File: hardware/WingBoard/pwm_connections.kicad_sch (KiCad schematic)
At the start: 11 parts

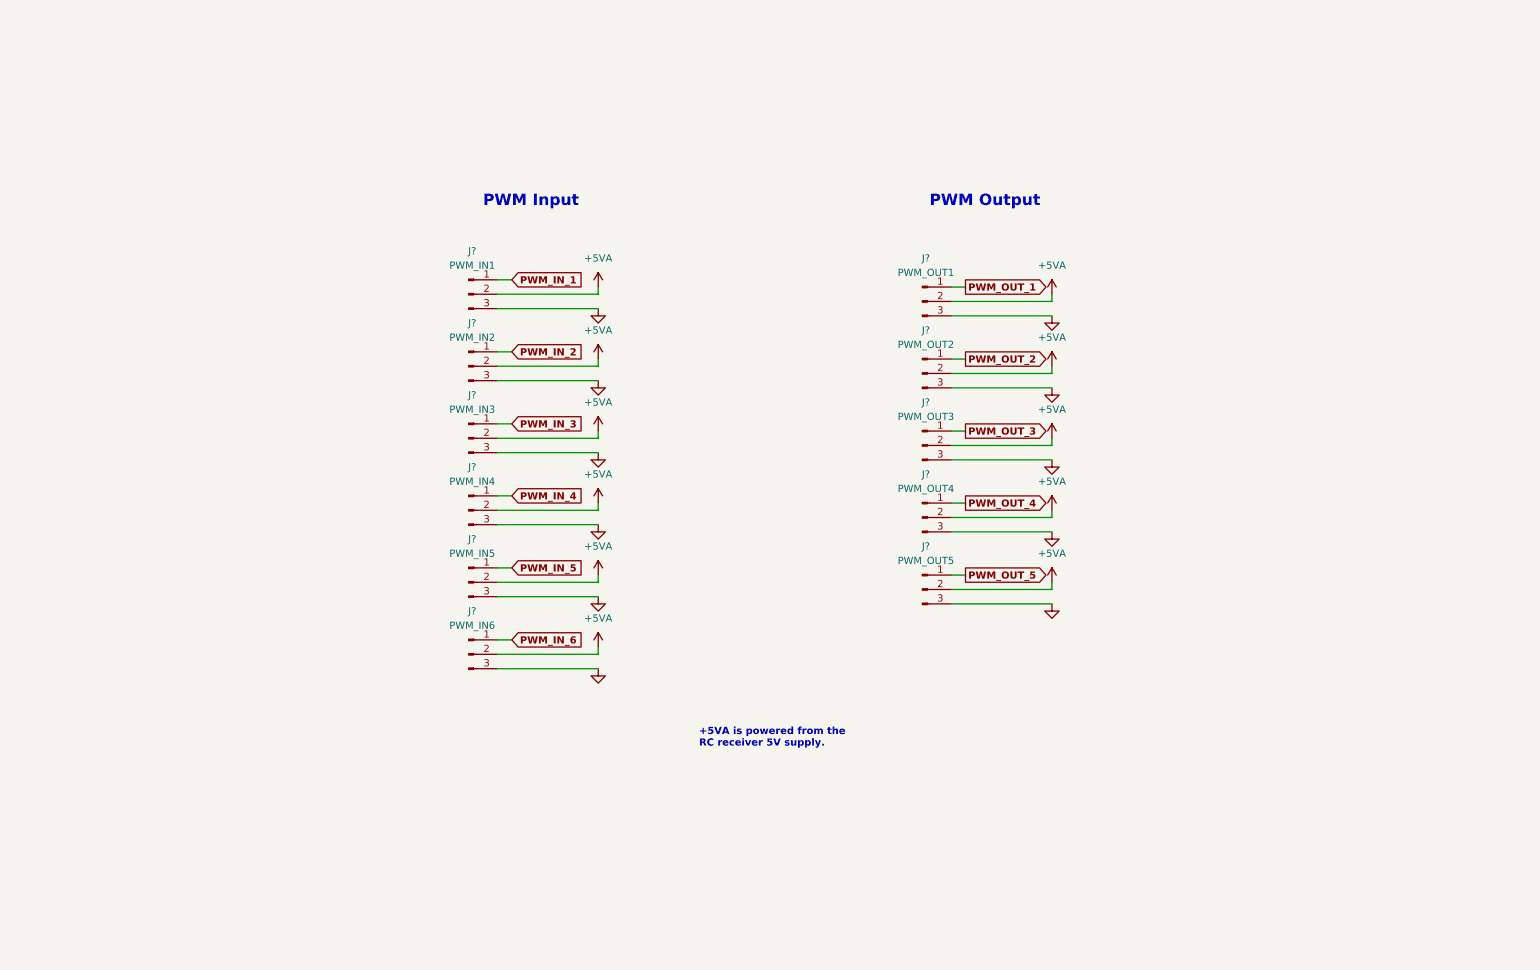
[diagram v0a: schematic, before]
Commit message: Added pwm controller.
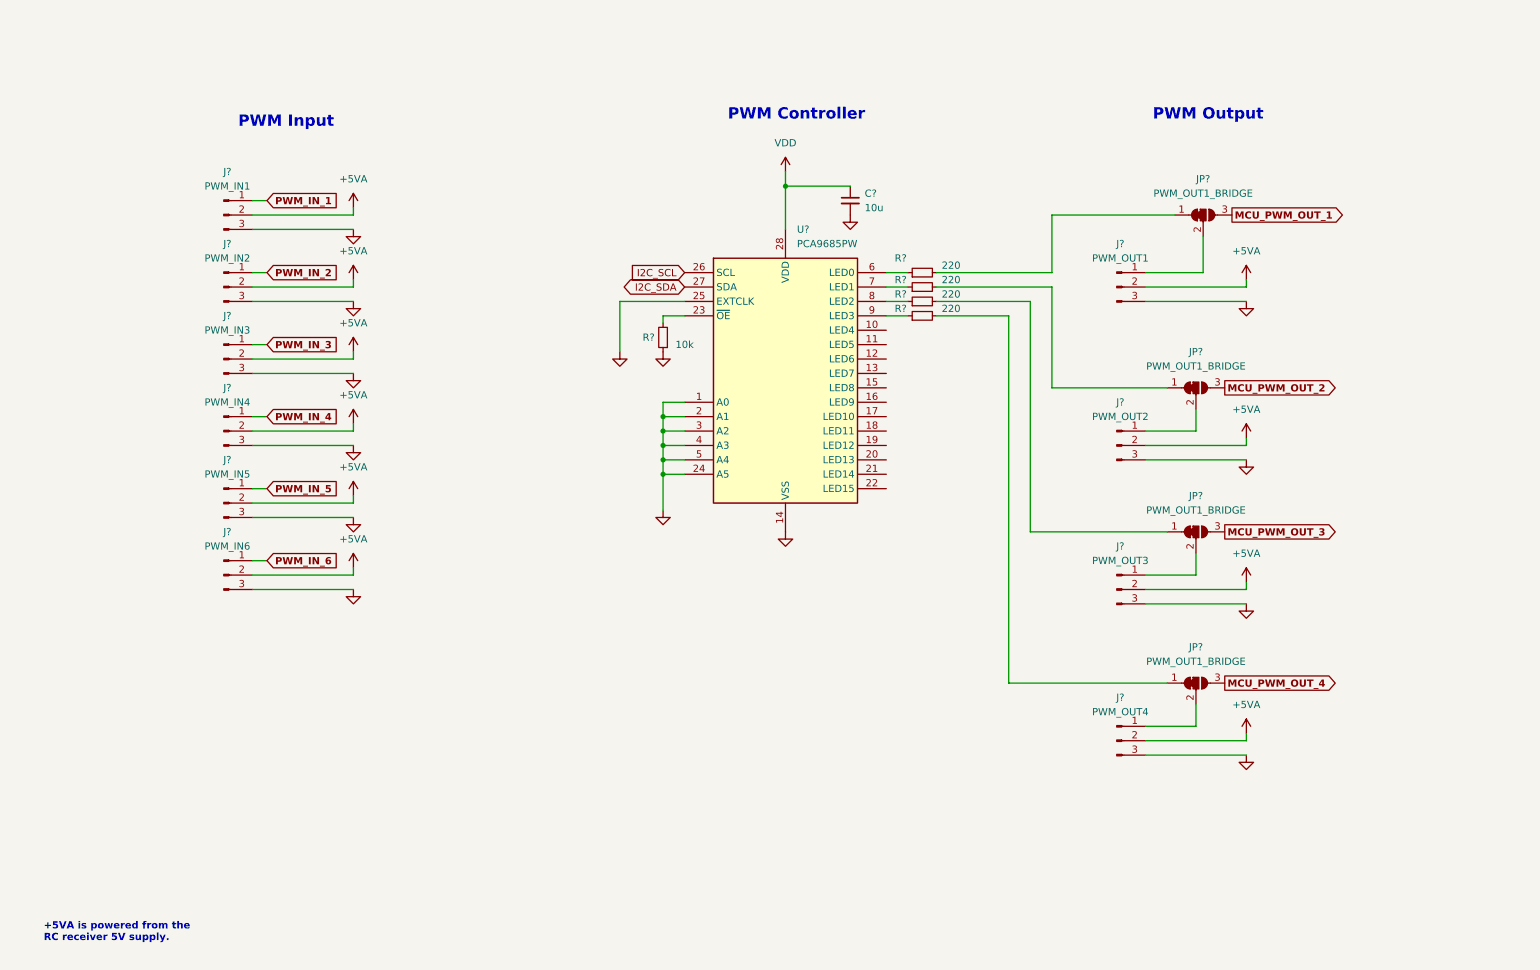
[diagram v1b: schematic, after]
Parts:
- removed J?: PWM_OUT5, symbol Connector:Conn_01x03_Male
- added C?: 10u, symbol Device:C_Small
- added JP? (x4): PWM_OUT1_BRIDGE, symbol Jumper:SolderJumper_3_Bridged12
- added R? (x4): 220, symbol Device:R_Small
- added R?: 10k, symbol Device:R_Small
- added U?: PCA9685PW, Package_SO:TSSOP-28_4.4x9.7mm_P0.65mm, symbol Driver_LED:PCA9685PW
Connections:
- net GND: now also C?.2, R?.1, U?.1 (A0), U?.14 (VSS), U?.2 (A1), U?.24 (A5), U?.25 (EXTCLK), U?.3 (A2), U?.4 (A3), U?.5 (A4)
- net PWM_OUT_1: no longer names the net of J?.1 (Pin_1)
- net PWM_OUT_1: now also JP?.2 (C)
- net PWM_OUT_2: no longer names the net of J?.1 (Pin_1)
- net PWM_OUT_2: now also JP?.2 (C)
- net PWM_OUT_3: no longer names the net of J?.1 (Pin_1)
- net PWM_OUT_3: now also JP?.2 (C)
- net PWM_OUT_4: no longer names the net of J?.1 (Pin_1)
- net PWM_OUT_4: now also JP?.2 (C)
- new net: JP?.1 (A), R?.2 (x4)
- new net: R?.2, U?.23 (~{OE})
- new net: R?.1, U?.6 (LED0)
- new net: R?.1, U?.7 (LED1)
- new net: R?.1, U?.8 (LED2)
- new net: R?.1, U?.9 (LED3)
- new net I2C_SCL: U?.26 (SCL)
- new net I2C_SDA: U?.27 (SDA)
- new net MCU_PWM_OUT_1: JP?.3 (B)
- new net MCU_PWM_OUT_2: JP?.3 (B)
- new net MCU_PWM_OUT_3: JP?.3 (B)
- new net MCU_PWM_OUT_4: JP?.3 (B)
- new net VDD: C?.1, U?.28 (VDD)
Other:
- note added: "PWM Controller"
- moved on the sheet: J?

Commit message: Hardware update: status LEDs, DIP switches, & test points.
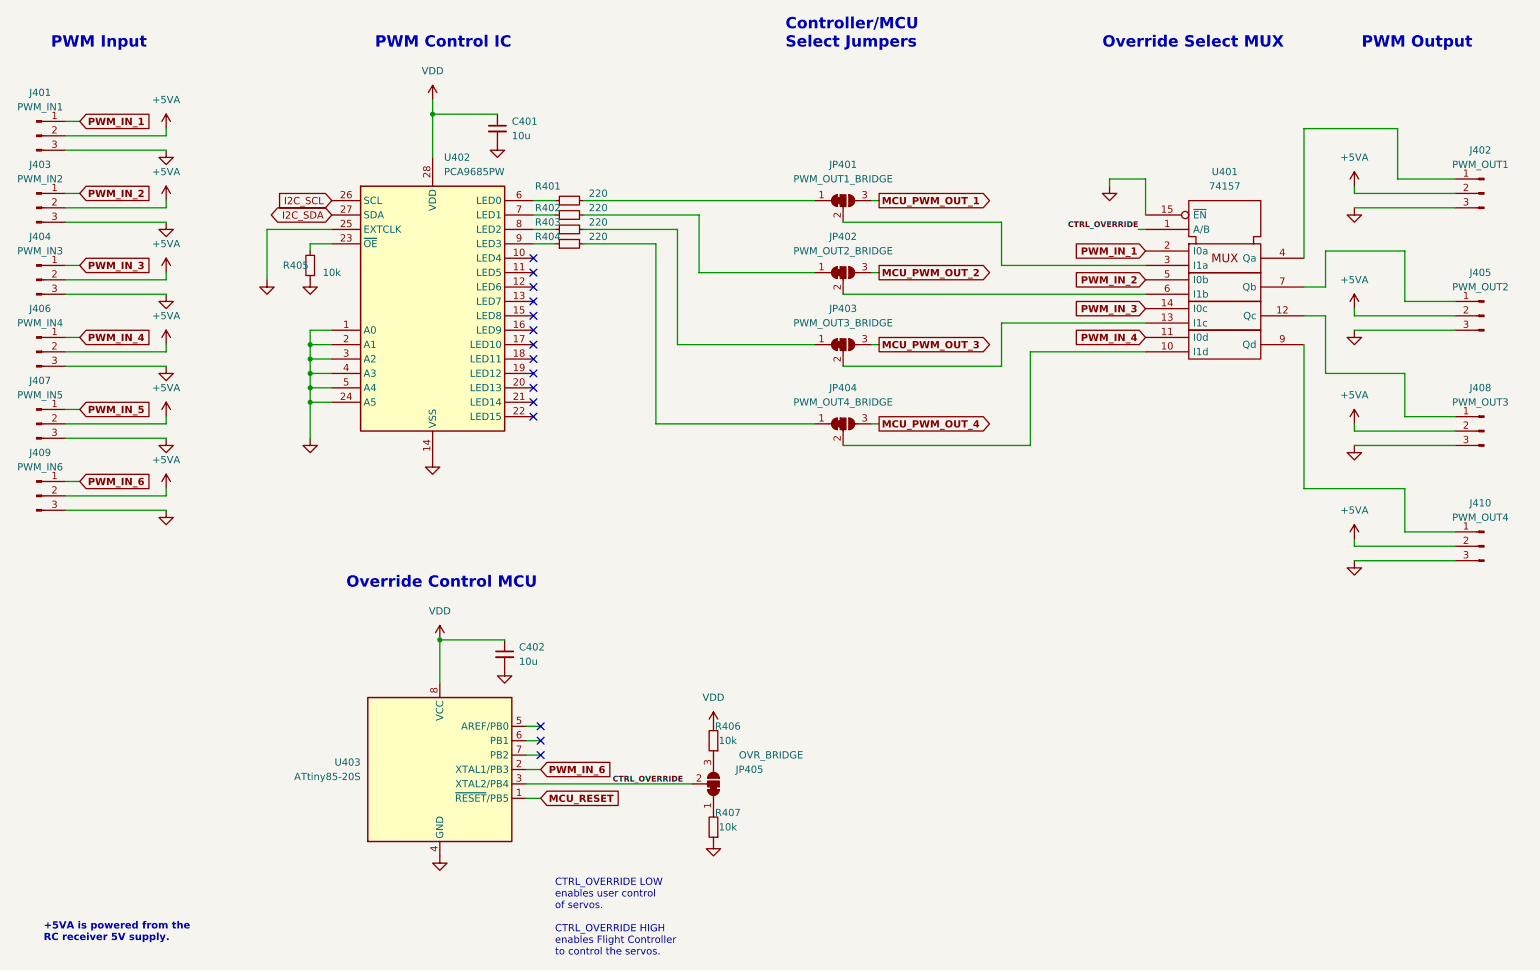
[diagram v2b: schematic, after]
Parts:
- added C402: 10u, symbol Device:C_Small
- added JP405: OVR_BRIDGE, symbol Jumper:SolderJumper_3_Bridged12
- added R406, R407: 10k, symbol Device:R_Small
- added U401: 74157, symbol 74xx_IEEE:74157
- added U403: ATtiny85-20S, Package_SO:SOIC-8W_5.3x5.3mm_P1.27mm, symbol MCU_Microchip_ATtiny:ATtiny85-20S
- JP402: renamed from JP?; value PWM_OUT1_BRIDGE -> PWM_OUT2_BRIDGE
- JP403: renamed from JP?; value PWM_OUT1_BRIDGE -> PWM_OUT3_BRIDGE
- JP404: renamed from JP?; value PWM_OUT1_BRIDGE -> PWM_OUT4_BRIDGE
- gave numbers to parts that had none: 18
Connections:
- net GND: now also C402.2, R407.1, U401.15 (~{EN}), U401.8 (GND), U403.4 (GND)
- net PWM_IN_1: now also U401.2 (I0a)
- net PWM_IN_2: now also U401.5 (I0b)
- net PWM_IN_3: now also U401.14 (I0c)
- net PWM_IN_4: now also U401.11 (I0d)
- net PWM_IN_6: now also U403.2 (XTAL1/PB3)
- net VDD: now also C402.1, R406.2, U403.8 (VCC)
- net at JP403.2 (C): now also U401.13 (I1c); no longer J408.1 (Pin_1)
- net at JP404.2 (C): now also U401.10 (I1d); no longer J410.1 (Pin_1)
- net at JP402.2 (C): now also U401.6 (I1b); no longer J405.1 (Pin_1)
- net at JP401.2 (C): now also U401.3 (I1a); no longer J402.1 (Pin_1)
- new net: JP405.1 (A), R407.2
- new net: JP405.3 (B), R406.1
- new net: J408.1 (Pin_1), U401.12 (Qc)
- new net: J402.1 (Pin_1), U401.4 (Qa)
- new net: J405.1 (Pin_1), U401.7 (Qb)
- new net: J410.1 (Pin_1), U401.9 (Qd)
- new net CTRL_OVERRIDE: JP405.2 (C), U401.1 (A/B), U403.3 (XTAL2/PB4)
- new net MCU_RESET: U403.1 (~{RESET}/PB5)
- new net VCC: U401.16 (VCC)
- no-connect marks 0 -> 15
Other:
- note added: "CTRL_OVERRIDE LOW enables user control of servos. CTRL_OVERRIDE HIGH enables Flight Controller to control the servos."
- note added: "Controller/MCU Select Jumpers"
- note added: "Override Control MCU"
- note added: "Override Select MUX"
- note added: "PWM Control IC"
- note removed: "PWM Controller"
- moved on the sheet: C401, J401, J402, J403, J404, J405, J406, J407, J408, J409, J410, JP401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

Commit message: Minor hardware design updates and assigned PCB footprints
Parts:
- added JP406: OVR BRIDGE, Resistor_SMD:R_0805_2012Metric_Pad1.20x1.40mm_HandSolder, symbol Jumper:SolderJumper_2_Bridged
- C401: footprint (none) -> Capacitor_SMD:C_0805_2012Metric_Pad1.18x1.45mm_HandSolder
- C402: value 10u -> 100n; footprint (none) -> Capacitor_SMD:C_0805_2012Metric_Pad1.18x1.45mm_HandSolder
- J401, J410: footprint (none) -> Connector_PinHeader_2.54mm:PinHeader_1x03_P2.54mm_Vertical
- J402: renamed from J403; footprint (none) -> Connector_PinHeader_2.54mm:PinHeader_1x03_P2.54mm_Vertical
- J403: renamed from J404; footprint (none) -> Connector_PinHeader_2.54mm:PinHeader_1x03_P2.54mm_Vertical
- J404: renamed from J406; footprint (none) -> Connector_PinHeader_2.54mm:PinHeader_1x03_P2.54mm_Vertical
- J405: renamed from J407; footprint (none) -> Connector_PinHeader_2.54mm:PinHeader_1x03_P2.54mm_Vertical
- J406: renamed from J409; footprint (none) -> Connector_PinHeader_2.54mm:PinHeader_1x03_P2.54mm_Vertical
- J407: renamed from J402; footprint (none) -> Connector_PinHeader_2.54mm:PinHeader_1x03_P2.54mm_Vertical
- J408: renamed from J405; footprint (none) -> Connector_PinHeader_2.54mm:PinHeader_1x03_P2.54mm_Vertical
- J409: renamed from J408; footprint (none) -> Connector_PinHeader_2.54mm:PinHeader_1x03_P2.54mm_Vertical
- JP401: renamed from JP405; value OVR_BRIDGE -> OVR UP/DOWN; footprint (none) -> Jumper:SolderJumper-3_P1.3mm_Bridged12_Pad1.0x1.5mm
- JP402: renamed from JP401; footprint (none) -> Jumper:SolderJumper-3_P1.3mm_Bridged12_Pad1.0x1.5mm
- JP403: renamed from JP402; footprint (none) -> Jumper:SolderJumper-3_P1.3mm_Bridged12_Pad1.0x1.5mm
- JP404: renamed from JP403; footprint (none) -> Jumper:SolderJumper-3_P1.3mm_Bridged12_Pad1.0x1.5mm
- JP405: renamed from JP404; footprint (none) -> Jumper:SolderJumper-3_P1.3mm_Bridged12_Pad1.0x1.5mm
- R401: renamed from R405; footprint (none) -> Resistor_SMD:R_0805_2012Metric_Pad1.20x1.40mm_HandSolder
- R402: renamed from R401; footprint (none) -> Resistor_SMD:R_0805_2012Metric_Pad1.20x1.40mm_HandSolder
- R403: renamed from R402; footprint (none) -> Resistor_SMD:R_0805_2012Metric_Pad1.20x1.40mm_HandSolder
- R404: renamed from R403; footprint (none) -> Resistor_SMD:R_0805_2012Metric_Pad1.20x1.40mm_HandSolder
- R405: renamed from R404; footprint (none) -> Resistor_SMD:R_0805_2012Metric_Pad1.20x1.40mm_HandSolder
- R406, R407: footprint (none) -> Resistor_SMD:R_0805_2012Metric_Pad1.20x1.40mm_HandSolder
- U403: renamed from U401; footprint (none) -> Proj ICs:SOP65P640X120-16N
- renumbered U402 to U401, U403 to U402
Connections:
- net CTRL_OVERRIDE: now also JP406.2 (B); no longer U402.3 (XTAL2/PB4)
- new net: JP406.1 (A), U402.3 (XTAL2/PB4)
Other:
- moved on the sheet: JP401, R406, R407

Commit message: PCB rough layout done.
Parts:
- added J411: PWM_OUT5, Connector_PinHeader_2.54mm:PinHeader_1x03_P2.54mm_Vertical, symbol Connector:Conn_01x03_Male
- added J412: PWM_OUT6, Connector_PinHeader_2.54mm:PinHeader_1x03_P2.54mm_Vertical, symbol Connector:Conn_01x03_Male
- added R408, R409: 220, Resistor_SMD:R_0805_2012Metric_Pad1.20x1.40mm_HandSolder, symbol Device:R_Small
- JP401: footprint Jumper:SolderJumper-3_P1.3mm_Bridged12_Pad1.0x1.5mm -> Jumper:SolderJumper-3_P1.3mm_Bridged2Bar12_Pad1.0x1.5mm
- JP406: footprint Resistor_SMD:R_0805_2012Metric_Pad1.20x1.40mm_HandSolder -> Jumper:SolderJumper-2_P1.3mm_Bridged2Bar_RoundedPad1.0x1.5mm
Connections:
- net +5VA: now also J411.2 (Pin_2), J412.2 (Pin_2)
- net GND: now also J411.3 (Pin_3), J412.3 (Pin_3)
- net PWM CTRL 2: now reaches JP404.1 (A), R404.2
- net PWM CTRL B2: now reaches JP404.2 (C), U403.13 (I1c)
- net PWM CTRL 3: now reaches JP405.1 (A), R405.2
- net PWM CTRL B3: now reaches JP405.2 (C), U403.10 (I1d)
- net at U401.10 (LED4): now also R408.1
- net at U401.11 (LED5): now also R409.1
- net PWM CTRL B0: now reaches JP402.2 (C), U403.3 (I1a)
- net PWM CTRL B1: now reaches JP403.2 (C), U403.6 (I1b)
- net PWM CTRL 0: now reaches JP402.1 (A), R402.2
- net PWM CTRL 1: now reaches JP403.1 (A), R403.2
- new net PWM_OUT5: J411.1 (Pin_1), R408.2
- new net PWM_OUT6: J412.1 (Pin_1), R409.2
- no-connect marks 15 -> 13
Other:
- note added: "Solder jumpers allow the FC MCU to directly control PWM out signals. This is a backup in case of there are issues with the PWM Control IC."
- note added: "The Override Select MUX allows the operator to resume direct control of the vehicle."
- note added: "This IC offloads PWM control from FC MCU. Channels 1-4 OUT are muxed with direct operator control. Channels 5-6 OUT are FC MCU control only."

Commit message: Hardware layout v0.1 complete.
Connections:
- net VCC is gone; now on net VDD: U403.16 (VDD)
- net PWM O3: now reaches J409.1 (Pin_1), U403.12 (Qc)
- net PWM O1: now reaches J407.1 (Pin_1), U403.4 (Qa)
- net PWM O2: now reaches J408.1 (Pin_1), U403.7 (Qb)
- net PWM O4: now reaches J410.1 (Pin_1), U403.9 (Qd)
- net PWM CTRL B0 renamed PWM TO MUX 1
- net PWM CTRL B1 renamed PWM TO MUX 2
- net PWM CTRL B2 renamed PWM TO MUX 3
- net PWM CTRL B3 renamed PWM TO MUX 4
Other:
- moved on the sheet: R408, R409
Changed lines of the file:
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@@
   (no_connect (at 111.76 149.86))
   (no_connect (at 111.76 152.4))
-  (wire (pts (xy 111.76 67.31) (xy 110.49 67.31))
+  (wire (pts (xy 114.3 67.31) (xy 110.49 67.31))
     (stroke (width 0) (type default) (color 0 0 0 0))
   )
@@
     (stroke (width 0) (type default) (color 0 0 0 0))
   )
-  (wire (pts (xy 111.76 64.77) (xy 110.49 64.77))
+  (wire (pts (xy 114.3 64.77) (xy 110.49 64.77))
     (stroke (width 0) (type default) (color 0 0 0 0))
   )
@@
     (stroke (width 0) (type default) (color 0 0 0 0))
   )
+  (wire (pts (xy 120.65 64.77) (xy 119.38 64.77))
+    (stroke (width 0) (type default) (color 0 0 0 0))
+  )
   (wire (pts (xy 165.1 71.12) (xy 218.44 71.12))
     (stroke (width 0) (type default) (color 0 0 0 0))
@@
   )
   (wire (pts (xy 193.04 83.82) (xy 193.04 76.2))
+    (stroke (width 0) (type default) (color 0 0 0 0))
+  )
+  (wire (pts (xy 120.65 67.31) (xy 119.38 67.31))
     (stroke (width 0) (type default) (color 0 0 0 0))
   )
@@
     (effects (font (size 2 2) bold) (justify left bottom))
   )
-  (label "PWM CTRL B0" (at 179.07 58.42 0)
+  (label "PWM TO MUX 1" (at 179.07 58.42 0)
     (effects (font (size 1.27 1.27)) (justify left bottom))
   )
@@
     (effects (font (size 1.27 1.27)) (justify left bottom))
   )
-  (label "PWM_OUT5" (at 116.84 64.77 0)
+  (label "PWM O4" (at 262.89 105.41 0)
+    (effects (font (size 1.27 1.27)) (justify left bottom))
+  )
+  (label "PWM_OUT5" (at 120.65 64.77 0)
     (effects (font (size 1 1)) (justify left bottom))
   )
-  (label "PWM_OUT6" (at 116.84 67.31 0)
+  (label "PWM_OUT6" (at 120.65 67.31 0)
     (effects (font (size 1 1)) (justify left bottom))
   )
@@
     (effects (font (size 1 1)) (justify right bottom))
   )
+  (label "PWM O3" (at 261.62 85.09 0)
+    (effects (font (size 1.27 1.27)) (justify left bottom))
+  )
+  (label "PWM O1" (at 259.08 41.91 0)
+    (effects (font (size 1.27 1.27)) (justify left bottom))
+  )
+  (label "PWM O2" (at 260.2511 63.5 0)
+    (effects (font (size 1.27 1.27)) (justify left bottom))
+  )
   (label "PWM CTRL 3" (at 129.54 62.23 0)
     (effects (font (size 1.27 1.27)) (justify left bottom))
   )
-  (label "PWM CTRL B2" (at 179.07 83.82 0)
+  (label "PWM TO MUX 3" (at 179.07 83.82 0)
     (effects (font (size 1.27 1.27)) (justify left bottom))
   )
@@
     (effects (font (size 1 1) bold) (justify left bottom))
   )
-  (label "PWM CTRL B3" (at 179.07 97.79 0)
+  (label "PWM TO MUX 4" (at 179.07 97.79 0)
     (effects (font (size 1.27 1.27)) (justify left bottom))
   )
-  (label "PWM CTRL B1" (at 179.07 71.12 0)
+  (label "PWM TO MUX 2" (at 179.07 71.12 0)
     (effects (font (size 1.27 1.27)) (justify left bottom))
   )
@@
     (pin "1")
   )
-  (symbol (lib_id "Device:R_Small") (at 114.3 64.77 90) (unit 1)
+  (symbol (lib_id "Device:R_Small") (at 116.84 64.77 90) (unit 1)
     (in_bom yes) (on_board yes)
-    (property "Reference" "R408" (id 0) (at 110.49 63.5 90))
-    (property "Value" "220" (id 1) (at 114.3 64.77 90))
-    (property "Footprint" "Resistor_SMD:R_0805_2012Metric_Pad1.20x1.40mm_HandSolder" (id 2) (at 114.3 64.77 0)
-      (effects (font (size 1.27 1.27)) hide)
-    )
-    (property "Datasheet" "~" (id 3) (at 114.3 64.77 0)
+    (property "Reference" "R408" (id 0) (at 113.03 63.5 90))
+    (property "Value" "220" (id 1) (at 116.84 64.77 90))
+    (property "Footprint" "Resistor_SMD:R_0805_2012Metric_Pad1.20x1.40mm_HandSolder" (id 2) (at 116.84 64.77 0)
+      (effects (font (size 1.27 1.27)) hide)
+    )
+    (property "Datasheet" "~" (id 3) (at 116.84 64.77 0)
       (effects (font (size 1.27 1.27)) hide)
     )
@@
     (pin "1")
   )
-  (symbol (lib_id "Device:R_Small") (at 114.3 67.31 90) (unit 1)
+  (symbol (lib_id "Device:R_Small") (at 116.84 67.31 90) (unit 1)
     (in_bom yes) (on_board yes)
-    (property "Reference" "R409" (id 0) (at 110.49 66.04 90))
-    (property "Value" "220" (id 1) (at 114.3 67.31 90))
-    (property "Footprint" "Resistor_SMD:R_0805_2012Metric_Pad1.20x1.40mm_HandSolder" (id 2) (at 114.3 67.31 0)
-      (effects (font (size 1.27 1.27)) hide)
-    )
-    (property "Datasheet" "~" (id 3) (at 114.3 67.31 0)
-      (effects (font (size 1.27 1.27)) hide)
-    )
+    (property "Reference" "R409" (id 0) (at 113.03 66.04 90))
+    (property "Value" "220" (id 1) (at 116.84 67.31 90))
+    (property "Footprint" "Resistor_SMD:R_0805_2012Metric_Pad1.20x1.40mm_HandSolder" (id 2) (at 116.84 67.31 0)
+      (effects (font (size 1.27 1.27)) hide)
+    )
+    (property "Datasheet" "~" (id 3) (at 116.84 67.31 0)
+      (effects (font (size 1.27 1.27)) hide)
+    )
